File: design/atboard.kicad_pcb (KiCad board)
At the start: 2 copper layers, 7 parts, among them J1 AVR_SPI, J2 Conn_01x14, J3 Conn_01x14, U1 ATmega328-PU, Y1 8 MHz

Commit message: connect the rest
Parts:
- added J4: POWER, Connector_JST:JST_PH_S2B-PH-K_1x02_P2.00mm_Horizontal, F.Cu at (73.7, 52.1)
- J2: value Conn_01x14 -> RIGHT_CONNECTOR
- J3: value Conn_01x14 -> LEFT_CONNECTOR
- moved C2 28.2 mm to (74.9, 59.7), turned to 270 degrees
- moved Y1 28.1 mm to (74.9, 81.3), turned to 90 degrees
- moved J2 24.0 mm to (95.2, 57.1)
- moved J1 23.7 mm to (91.4, 48.3), turned to 270 degrees
- moved C1 19.4 mm to (74.9, 68.6), turned to 90 degrees
- moved J3 7.81 mm to (69.8, 57.1)
- moved U1 4.24 mm to (81.3, 57.1)
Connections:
- J1 pad 3: Net-(J1-Pad3) -> /SCK
- J1 pad 4: Net-(J1-Pad4) -> /MOSI
- J1 pad 5: Net-(J1-Pad5) -> /RST
- J2 pad 1: Net-(J2-Pad1) -> /28
- J2 pad 10: Net-(J2-Pad10) -> /SCK
- J2 pad 11: Net-(J2-Pad11) -> /MISO
- J2 pad 12: Net-(J2-Pad12) -> /MOSI
- J2 pad 13: Net-(J2-Pad13) -> /16
- J2 pad 14: Net-(J2-Pad14) -> /15
- J2 pad 2: Net-(J2-Pad2) -> /27
- J2 pad 3: Net-(J2-Pad3) -> /26
- J2 pad 4: Net-(J2-Pad4) -> /25
- J2 pad 5: Net-(J2-Pad5) -> /24
- J2 pad 6: Net-(J2-Pad6) -> /23
- J2 pad 7: Net-(J2-Pad7) -> GND
- J2 pad 8: Net-(J2-Pad8) -> /21
- J2 pad 9: Net-(J2-Pad9) -> /20
- J3 pad 10: Net-(J3-Pad10) -> /10
- J3 pad 11: Net-(J3-Pad11) -> /11
- J3 pad 12: Net-(J3-Pad12) -> /12
- J3 pad 13: Net-(J3-Pad13) -> /13
- J3 pad 14: Net-(J3-Pad14) -> /14
- J3 pad 9: Net-(J3-Pad9) -> /9
- U1 pad 14: Net-(U1-Pad14) -> /14
- U1 pad 15: Net-(U1-Pad15) -> /15
- U1 pad 16: Net-(U1-Pad16) -> /16
- U1 pad 17: Net-(U1-Pad17) -> /MOSI
- U1 pad 18: Net-(U1-Pad18) -> /MISO
- U1 pad 19: Net-(U1-Pad19) -> /SCK
- U1 pad 20: Net-(U1-Pad20) -> /20
- U1 pad 21: Net-(U1-Pad21) -> /21
- U1 pad 23: Net-(U1-Pad23) -> /23
- U1 pad 24: Net-(U1-Pad24) -> /24
- U1 pad 25: Net-(U1-Pad25) -> /25
- U1 pad 26: Net-(U1-Pad26) -> /26
- U1 pad 27: Net-(U1-Pad27) -> /27
- U1 pad 28: Net-(U1-Pad28) -> /28

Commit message: added board edge
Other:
- board outline added: 36.8 x 53.3 mm
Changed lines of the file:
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@@
-(kicad_pcb (version 20171130) (host pcbnew "(5.1.0-0)")
+(kicad_pcb (version 20171130) (host pcbnew "(5.1.0)-1")
   (general
     (thickness 1.6)
-    (drawings 0)
+    (drawings 4)
     (tracks 0)
     (zones 0)
@@
     (solder_mask_min_width 0.25)
     (aux_axis_origin 0 0)
-    (visible_elements FFFFFF7F)
+    (visible_elements 7FFFFFFF)
     (pcbplotparams
       (layerselection 0x010fc_ffffffff)
@@
       (effects (font (size 1 1) (thickness 0.15)))
     )
-    (fp_text value RIGHT_CONNECTOR (at 0 35.35) (layer F.Fab)
+    (fp_text value RIGHT_CONNECTOR (at 2.54 24.13 90) (layer F.Fab)
       (effects (font (size 1 1) (thickness 0.15)))
     )
@@
       (effects (font (size 1 1) (thickness 0.15)))
     )
-    (fp_text value LEFT_CONNECTOR (at 0 35.35) (layer F.Fab)
+    (fp_text value LEFT_CONNECTOR (at -3.81 17.78 90) (layer F.Fab)
       (effects (font (size 1 1) (thickness 0.15)))
     )
@@
     )
   )
+  (gr_line (start 100.33 41.91) (end 63.5 41.91) (layer Edge.Cuts) (width 0.1))
+  (gr_line (start 100.33 95.25) (end 100.33 41.91) (layer Edge.Cuts) (width 0.1))
+  (gr_line (start 63.5 95.25) (end 100.33 95.25) (layer Edge.Cuts) (width 0.1))
+  (gr_line (start 63.5 41.91) (end 63.5 95.25) (layer Edge.Cuts) (width 0.1))
 )

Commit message: added power net group
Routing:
- net GND: track 0.00 -> 66.9 mm
- net +3V3: track 0.00 -> 37.1 mm, vias 0 -> 1
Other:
- net class Power added: clearance 0.3, trace_width 0.4, via_dia 0.9, via_drill 0.4
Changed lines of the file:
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@@
     (thickness 1.6)
     (drawings 4)
-    (tracks 0)
+    (tracks 24)
     (zones 0)
     (modules 8)
@@
     (uvia_dia 0.3)
     (uvia_drill 0.1)
-    (add_net +3V3)
-    (add_net +5V)
     (add_net /10)
     (add_net /11)
@@
     (add_net /RST)
     (add_net /SCK)
+  )
+  (net_class Power ""
+    (clearance 0.3)
+    (trace_width 0.4)
+    (via_dia 0.9)
+    (via_drill 0.4)
+    (uvia_dia 0.4)
+    (uvia_drill 0.1)
+    (add_net +3V3)
+    (add_net +5V)
     (add_net GND)
   )
@@
   (gr_line (start 63.5 95.25) (end 100.33 95.25) (layer Edge.Cuts) (width 0.1))
   (gr_line (start 63.5 41.91) (end 63.5 95.25) (layer Edge.Cuts) (width 0.1))
+  (segment (start 88.9 72.39) (end 95.25 72.39) (width 0.25) (layer F.Cu) (net 1))
+  (segment (start 83.82 72.39) (end 81.28 74.93) (width 0.25) (layer F.Cu) (net 1))
+  (segment (start 88.9 72.39) (end 83.82 72.39) (width 0.25) (layer F.Cu) (net 1))
+  (segment (start 85.496401 51.663599) (end 86.36 50.8) (width 0.4) (layer F.Cu) (net 1))
+  (segment (start 83.71499 53.44501) (end 85.496401 51.663599) (width 0.4) (layer F.Cu) (net 1))
+  (segment (start 72.76001 53.44501) (end 83.71499 53.44501) (width 0.4) (layer F.Cu) (net 1))
+  (segment (start 71.66 52.345) (end 72.76001 53.44501) (width 0.4) (layer F.Cu) (net 1))
+  (segment (start 71.66 52.07) (end 71.66 52.345) (width 0.4) (layer F.Cu) (net 1))
+  (segment (start 71.66 58.92) (end 74.93 62.19) (width 0.4) (layer F.Cu) (net 1))
+  (segment (start 71.66 52.07) (end 71.66 58.92) (width 0.4) (layer F.Cu) (net 1))
+  (segment (start 74.93 62.19) (end 74.93 66.08) (width 0.4) (layer F.Cu) (net 1))
+  (segment (start 80.480001 74.130001) (end 81.28 74.93) (width 0.4) (layer F.Cu) (net 1))
+  (segment (start 76.230001 69.880001) (end 80.480001 74.130001) (width 0.4) (layer F.Cu) (net 1))
+  (segment (start 76.230001 67.380001) (end 76.230001 69.880001) (width 0.4) (layer F.Cu) (net 1))
+  (segment (start 74.93 66.08) (end 76.230001 67.380001) (width 0.4) (layer F.Cu) (net 1))
+  (segment (start 74.899999 69.880001) (end 69.85 74.93) (width 0.4) (layer F.Cu) (net 1))
+  (segment (start 76.230001 69.880001) (end 74.899999 69.880001) (width 0.4) (layer F.Cu) (net 1))
+  (via (at 77.47 52.07) (size 0.9) (drill 0.4) (layers F.Cu B.Cu) (net 12))
+  (segment (start 73.66 52.07) (end 77.47 52.07) (width 0.4) (layer F.Cu) (net 12))
+  (segment (start 80.480001 71.590001) (end 81.28 72.39) (width 0.4) (layer B.Cu) (net 12))
+  (segment (start 79.979999 71.089999) (end 80.480001 71.590001) (width 0.4) (layer B.Cu) (net 12))
+  (segment (start 79.979999 54.579999) (end 79.979999 71.089999) (width 0.4) (layer B.Cu) (net 12))
+  (segment (start 77.47 52.07) (end 79.979999 54.579999) (width 0.4) (layer B.Cu) (net 12))
+  (segment (start 81.28 72.39) (end 69.85 72.39) (width 0.4) (layer B.Cu) (net 12))
 )

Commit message: routing is hard
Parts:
- moved Y1 17.7 mm to (68.6, 64.8)
- moved C2 11.8 mm to (67.0, 51.0)
- moved C1 11.5 mm to (70.0, 79.0)
- moved J3 6.35 mm to (76.2, 57.1)
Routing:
- net GND: track 66.9 -> 6.62 mm
- net +3V3: track 37.1 -> 25.7 mm
- net /9: track 0.00 -> 11.2 mm
- net /RST: track 0.00 -> 11.0 mm
- net /10: track 0.00 -> 6.62 mm
- net /SCK: track 0.00 -> 6.35 mm
- net /MOSI: track 0.00 -> 6.35 mm
- net /MISO: track 0.00 -> 6.35 mm
- net /28: track 0.00 -> 6.35 mm
- net /27: track 0.00 -> 6.35 mm
- net /26: track 0.00 -> 6.35 mm
- net /25: track 0.00 -> 6.35 mm
- net /24: track 0.00 -> 6.35 mm
- net /23: track 0.00 -> 6.35 mm
- net /21: track 0.00 -> 6.35 mm
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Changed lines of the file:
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@@
-(kicad_pcb (version 20171130) (host pcbnew "(5.1.0)-1")
+(kicad_pcb (version 20171130) (host pcbnew "(5.1.0-0)")
   (general
     (thickness 1.6)
     (drawings 4)
-    (tracks 24)
+    (tracks 30)
     (zones 0)
     (modules 8)
@@
     (add_net GND)
   )
-  (module Crystal:Crystal_HC49-4H_Vertical (layer F.Cu)
-    (at 74.93 81.28 90)
+  (module Crystal:Crystal_HC49-4H_Vertical placed (layer F.Cu)
+    (at 68.58 64.77 90)
     (descr "Crystal THT HC-49-4H http://5hertz.com/pdfs/04404_D.pdf")
     (tags "THT crystalHC-49-4H")
@@
     )
   )
-  (module Capacitor_THT:C_Disc_D3.0mm_W2.0mm_P2.50mm (layer F.Cu)
-    (at 74.93 68.58 90)
+  (module Capacitor_THT:C_Disc_D3.0mm_W2.0mm_P2.50mm placed (layer F.Cu)
+    (at 70 79 90)
     (descr "C, Disc series, Radial, pin pitch=2.50mm, , diameter*width=3*2mm^2, Capacitor")
     (tags "C Disc series Radial pin pitch 2.50mm  diameter 3mm width 2mm Capacitor")
@@
     )
   )
-  (module Capacitor_THT:C_Disc_D3.0mm_W2.0mm_P2.50mm (layer F.Cu)
-    (at 74.93 59.69 270)
+  (module Capacitor_THT:C_Disc_D3.0mm_W2.0mm_P2.50mm placed (layer F.Cu)
+    (at 67 51 270)
     (descr "C, Disc series, Radial, pin pitch=2.50mm, , diameter*width=3*2mm^2, Capacitor")
     (tags "C Disc series Radial pin pitch 2.50mm  diameter 3mm width 2mm Capacitor")
@@
   )
   (module Connector_PinHeader_2.54mm:PinHeader_1x14_P2.54mm_Vertical (layer F.Cu)
-    (at 69.85 57.15)
+    (at 76.2 57.15)
     (descr "Through hole straight pin header, 1x14, 2.54mm pitch, single row")
     (tags "Through hole pin header THT 1x14 2.54mm single row")
@@
       (effects (font (size 1 1) (thickness 0.15)))
     )
-    (fp_text value LEFT_CONNECTOR (at -3.81 17.78 90) (layer F.Fab)
+    (fp_text value LEFT_CONNECTOR (at -2.54 29.21 90) (layer F.Fab) hide
       (effects (font (size 1 1) (thickness 0.15)))
     )
@@
   (gr_line (start 63.5 41.91) (end 63.5 95.25) (layer Edge.Cuts) (width 0.1))
   (segment (start 88.9 72.39) (end 95.25 72.39) (width 0.25) (layer F.Cu) (net 1))
-  (segment (start 83.82 72.39) (end 81.28 74.93) (width 0.25) (layer F.Cu) (net 1))
-  (segment (start 88.9 72.39) (end 83.82 72.39) (width 0.25) (layer F.Cu) (net 1))
-  (segment (start 85.496401 51.663599) (end 86.36 50.8) (width 0.4) (layer F.Cu) (net 1))
-  (segment (start 83.71499 53.44501) (end 85.496401 51.663599) (width 0.4) (layer F.Cu) (net 1))
-  (segment (start 72.76001 53.44501) (end 83.71499 53.44501) (width 0.4) (layer F.Cu) (net 1))
-  (segment (start 71.66 52.345) (end 72.76001 53.44501) (width 0.4) (layer F.Cu) (net 1))
   (segment (start 71.66 52.07) (end 71.66 52.345) (width 0.4) (layer F.Cu) (net 1))
-  (segment (start 71.66 58.92) (end 74.93 62.19) (width 0.4) (layer F.Cu) (net 1))
-  (segment (start 71.66 52.07) (end 71.66 58.92) (width 0.4) (layer F.Cu) (net 1))
-  (segment (start 74.93 62.19) (end 74.93 66.08) (width 0.4) (layer F.Cu) (net 1))
-  (segment (start 80.480001 74.130001) (end 81.28 74.93) (width 0.4) (layer F.Cu) (net 1))
-  (segment (start 76.230001 69.880001) (end 80.480001 74.130001) (width 0.4) (layer F.Cu) (net 1))
-  (segment (start 76.230001 67.380001) (end 76.230001 69.880001) (width 0.4) (layer F.Cu) (net 1))
-  (segment (start 74.93 66.08) (end 76.230001 67.380001) (width 0.4) (layer F.Cu) (net 1))
-  (segment (start 74.899999 69.880001) (end 69.85 74.93) (width 0.4) (layer F.Cu) (net 1))
-  (segment (start 76.230001 69.880001) (end 74.899999 69.880001) (width 0.4) (layer F.Cu) (net 1))
+  (segment (start 75.19 79) (end 76.2 80.01) (width 0.25) (layer F.Cu) (net 2))
+  (segment (start 70 79) (end 75.19 79) (width 0.25) (layer F.Cu) (net 2))
+  (segment (start 67 51) (end 65.84 51) (width 0.25) (layer F.Cu) (net 3))
+  (segment (start 65.774999 57.084999) (end 67.830001 59.140001) (width 0.25) (layer F.Cu) (net 3))
+  (segment (start 65.774999 51.065001) (end 65.774999 57.084999) (width 0.25) (layer F.Cu) (net 3))
+  (segment (start 67.830001 59.140001) (end 68.58 59.89) (width 0.25) (layer F.Cu) (net 3))
+  (segment (start 65.84 51) (end 65.774999 51.065001) (width 0.25) (layer F.Cu) (net 3))
+  (segment (start 88.9 82.55) (end 95.25 82.55) (width 0.25) (layer F.Cu) (net 4))
+  (segment (start 81.28 53.34) (end 81.28 57.15) (width 0.25) (layer F.Cu) (net 6))
+  (segment (start 86.36 48.26) (end 81.28 53.34) (width 0.25) (layer F.Cu) (net 6))
   (via (at 77.47 52.07) (size 0.9) (drill 0.4) (layers F.Cu B.Cu) (net 12))
   (segment (start 73.66 52.07) (end 77.47 52.07) (width 0.4) (layer F.Cu) (net 12))
@@
   (segment (start 79.979999 54.579999) (end 79.979999 71.089999) (width 0.4) (layer B.Cu) (net 12))
   (segment (start 77.47 52.07) (end 79.979999 54.579999) (width 0.4) (layer B.Cu) (net 12))
-  (segment (start 81.28 72.39) (end 69.85 72.39) (width 0.4) (layer B.Cu) (net 12))
+  (segment (start 88.9 80.01) (end 95.25 80.01) (width 0.25) (layer F.Cu) (net 16))
+  (segment (start 88.9 85.09) (end 95.25 85.09) (width 0.25) (layer F.Cu) (net 17))
+  (segment (start 88.9 90.17) (end 95.25 90.17) (width 0.25) (layer F.Cu) (net 18))
+  (segment (start 88.9 87.63) (end 95.25 87.63) (width 0.25) (layer F.Cu) (net 19))
+  (segment (start 88.9 77.47) (end 95.25 77.47) (width 0.25) (layer F.Cu) (net 20))
+  (segment (start 88.9 74.93) (end 95.25 74.93) (width 0.25) (layer F.Cu) (net 21))
+  (segment (start 88.9 69.85) (end 95.25 69.85) (width 0.25) (layer F.Cu) (net 22))
+  (segment (start 88.9 67.31) (end 95.25 67.31) (width 0.25) (layer F.Cu) (net 23))
+  (segment (start 88.9 64.77) (end 95.25 64.77) (width 0.25) (layer F.Cu) (net 24))
+  (segment (start 88.9 62.23) (end 95.25 62.23) (width 0.25) (layer F.Cu) (net 25))
+  (segment (start 88.9 59.69) (end 95.25 59.69) (width 0.25) (layer F.Cu) (net 26))
+  (segment (start 88.9 57.15) (end 95.25 57.15) (width 0.25) (layer F.Cu) (net 27))
 )

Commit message: save work
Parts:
- moved J2 2.54 mm to (92.7, 57.1)
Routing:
- net GND: track 6.62 -> 0.27 mm
- net /SCK: track 6.35 -> 0.00 mm
- net /MOSI: track 6.35 -> 0.00 mm
- net /MISO: track 6.35 -> 0.00 mm
- net /28: track 6.35 -> 0.00 mm
- net /27: track 6.35 -> 0.00 mm
- net /26: track 6.35 -> 0.00 mm
- net /25: track 6.35 -> 0.00 mm
- net /24: track 6.35 -> 0.00 mm
- net /23: track 6.35 -> 0.00 mm
- net /21: track 6.35 -> 0.00 mm
- net /20: track 6.35 -> 0.00 mm
- net /16: track 6.35 -> 0.00 mm
- net /15: track 6.35 -> 0.00 mm
- net /RST: track 11.0 -> 16.1 mm
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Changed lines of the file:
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@@
     (thickness 1.6)
     (drawings 4)
-    (tracks 30)
+    (tracks 28)
     (zones 0)
     (modules 8)
@@
       (effects (font (size 1 1) (thickness 0.15)))
     )
-    (fp_text value AVR_SPI (at 1.27 11.684 270) (layer F.Fab)
+    (fp_text value AVR_SPI (at -5.08 2.54) (layer F.Fab)
       (effects (font (size 1 1) (thickness 0.15)))
     )
@@
   )
   (module Connector_PinHeader_2.54mm:PinHeader_1x14_P2.54mm_Vertical (layer F.Cu)
-    (at 95.25 57.15)
+    (at 92.71 57.15)
     (descr "Through hole straight pin header, 1x14, 2.54mm pitch, single row")
     (tags "Through hole pin header THT 1x14 2.54mm single row")
@@
   (gr_line (start 63.5 95.25) (end 100.33 95.25) (layer Edge.Cuts) (width 0.1))
   (gr_line (start 63.5 41.91) (end 63.5 95.25) (layer Edge.Cuts) (width 0.1))
-  (segment (start 88.9 72.39) (end 95.25 72.39) (width 0.25) (layer F.Cu) (net 1))
   (segment (start 71.66 52.07) (end 71.66 52.345) (width 0.4) (layer F.Cu) (net 1))
   (segment (start 75.19 79) (end 76.2 80.01) (width 0.25) (layer F.Cu) (net 2))
   (segment (start 70 79) (end 75.19 79) (width 0.25) (layer F.Cu) (net 2))
+  (segment (start 81.28 80.01) (end 76.2 80.01) (width 0.25) (layer F.Cu) (net 2))
   (segment (start 67 51) (end 65.84 51) (width 0.25) (layer F.Cu) (net 3))
   (segment (start 65.774999 57.084999) (end 67.830001 59.140001) (width 0.25) (layer F.Cu) (net 3))
@@
   (segment (start 67.830001 59.140001) (end 68.58 59.89) (width 0.25) (layer F.Cu) (net 3))
   (segment (start 65.84 51) (end 65.774999 51.065001) (width 0.25) (layer F.Cu) (net 3))
-  (segment (start 88.9 82.55) (end 95.25 82.55) (width 0.25) (layer F.Cu) (net 4))
+  (segment (start 81.28 77.47) (end 76.2 77.47) (width 0.25) (layer F.Cu) (net 3))
   (segment (start 81.28 53.34) (end 81.28 57.15) (width 0.25) (layer F.Cu) (net 6))
   (segment (start 86.36 48.26) (end 81.28 53.34) (width 0.25) (layer F.Cu) (net 6))
+  (segment (start 81.28 57.15) (end 76.2 57.15) (width 0.25) (layer F.Cu) (net 6))
+  (segment (start 81.28 59.69) (end 76.2 59.69) (width 0.25) (layer F.Cu) (net 7))
+  (segment (start 81.28 62.23) (end 76.2 62.23) (width 0.25) (layer F.Cu) (net 8))
+  (segment (start 81.28 64.77) (end 76.2 64.77) (width 0.25) (layer F.Cu) (net 9))
+  (segment (start 81.28 67.31) (end 76.2 67.31) (width 0.25) (layer F.Cu) (net 10))
+  (segment (start 81.28 69.85) (end 76.2 69.85) (width 0.25) (layer F.Cu) (net 11))
   (via (at 77.47 52.07) (size 0.9) (drill 0.4) (layers F.Cu B.Cu) (net 12))
   (segment (start 73.66 52.07) (end 77.47 52.07) (width 0.4) (layer F.Cu) (net 12))
@@
   (segment (start 79.979999 54.579999) (end 79.979999 71.089999) (width 0.4) (layer B.Cu) (net 12))
   (segment (start 77.47 52.07) (end 79.979999 54.579999) (width 0.4) (layer B.Cu) (net 12))
-  (segment (start 88.9 80.01) (end 95.25 80.01) (width 0.25) (layer F.Cu) (net 16))
-  (segment (start 88.9 85.09) (end 95.25 85.09) (width 0.25) (layer F.Cu) (net 17))
-  (segment (start 88.9 90.17) (end 95.25 90.17) (width 0.25) (layer F.Cu) (net 18))
-  (segment (start 88.9 87.63) (end 95.25 87.63) (width 0.25) (layer F.Cu) (net 19))
-  (segment (start 88.9 77.47) (end 95.25 77.47) (width 0.25) (layer F.Cu) (net 20))
-  (segment (start 88.9 74.93) (end 95.25 74.93) (width 0.25) (layer F.Cu) (net 21))
-  (segment (start 88.9 69.85) (end 95.25 69.85) (width 0.25) (layer F.Cu) (net 22))
-  (segment (start 88.9 67.31) (end 95.25 67.31) (width 0.25) (layer F.Cu) (net 23))
-  (segment (start 88.9 64.77) (end 95.25 64.77) (width 0.25) (layer F.Cu) (net 24))
-  (segment (start 88.9 62.23) (end 95.25 62.23) (width 0.25) (layer F.Cu) (net 25))
-  (segment (start 88.9 59.69) (end 95.25 59.69) (width 0.25) (layer F.Cu) (net 26))
-  (segment (start 88.9 57.15) (end 95.25 57.15) (width 0.25) (layer F.Cu) (net 27))
+  (segment (start 81.28 82.55) (end 76.2 82.55) (width 0.25) (layer F.Cu) (net 13))
+  (segment (start 81.28 85.09) (end 76.2 85.09) (width 0.25) (layer F.Cu) (net 14))
+  (segment (start 81.28 87.63) (end 76.2 87.63) (width 0.25) (layer F.Cu) (net 15))
+  (segment (start 81.28 90.17) (end 76.2 90.17) (width 0.25) (layer F.Cu) (net 28))
 )

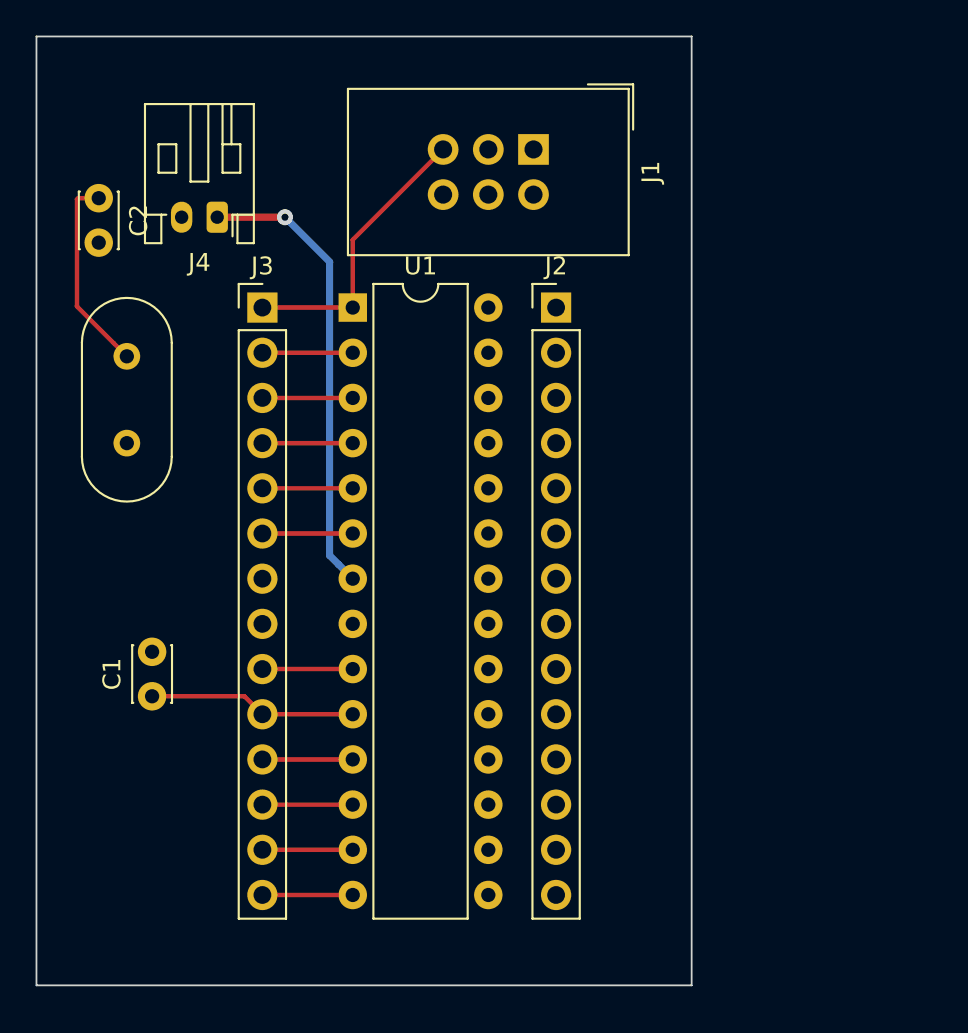
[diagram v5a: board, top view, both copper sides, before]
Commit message: got most of the board routed. GND is on layer 2
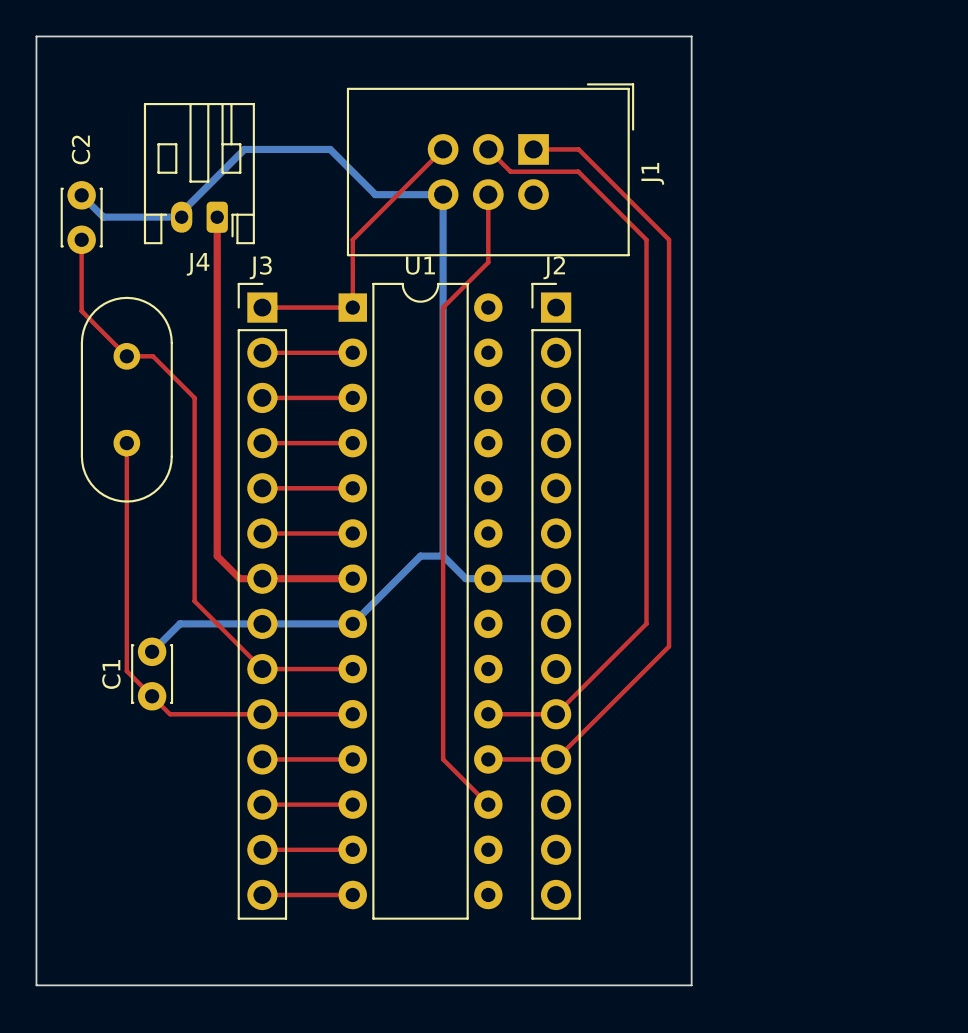
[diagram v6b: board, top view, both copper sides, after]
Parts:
- moved C2 2.53 mm to (66.0, 53.3), turned to 90 degrees
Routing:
- net GND: track 0.27 -> 69.7 mm
- net /MISO: track 0.00 -> 45.4 mm
- net /SCK: track 0.00 -> 43.6 mm
- net /MOSI: track 0.00 -> 36.4 mm
- net /9: track 16.3 -> 34.3 mm
- net /10: track 11.7 -> 26.5 mm
- net +3V3: track 25.7 -> 27.2 mm, vias 1 -> 0
